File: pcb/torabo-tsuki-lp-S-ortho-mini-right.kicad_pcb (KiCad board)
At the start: 2 copper layers, 138.8 x 74 mm, 59 parts, among them J201 Conn_01x06_MountingPin, J202 FTSH-106-01-L-D-K, SW43 SW_Push, SW44 SW_Push, SW45 SW_Push, SW46 SW_Push, SW47 SW_Push, SW48 SW_Push, SW50 SW_Push, SW51 SW_Push, SW52 SW_Push, SW53 SW_Push, SW54 SW_Push, SW55 SW_Push, SW57 SW_Push, SW58 SW_Push, SW59 SW_Push, SW60 SW_Push, SW61 SW_Push, SW62 SW_Push, SW63 SW_Push, SW64 SW_Push, SW65 SW_Push, SW69 SW_Push, SW70 SW_Push, U201 XIAO nRF52840 Plus

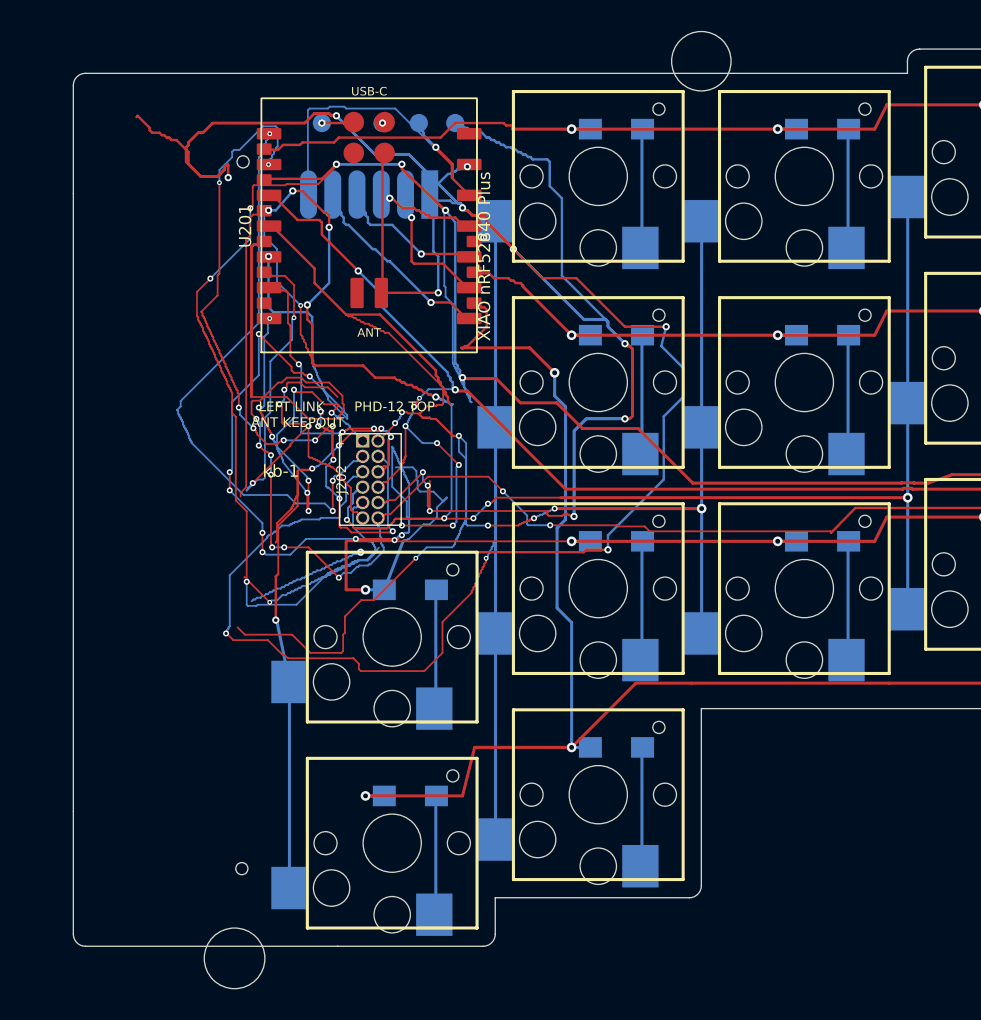
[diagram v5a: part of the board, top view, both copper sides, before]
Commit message: Shrink inner edges of split PCBs
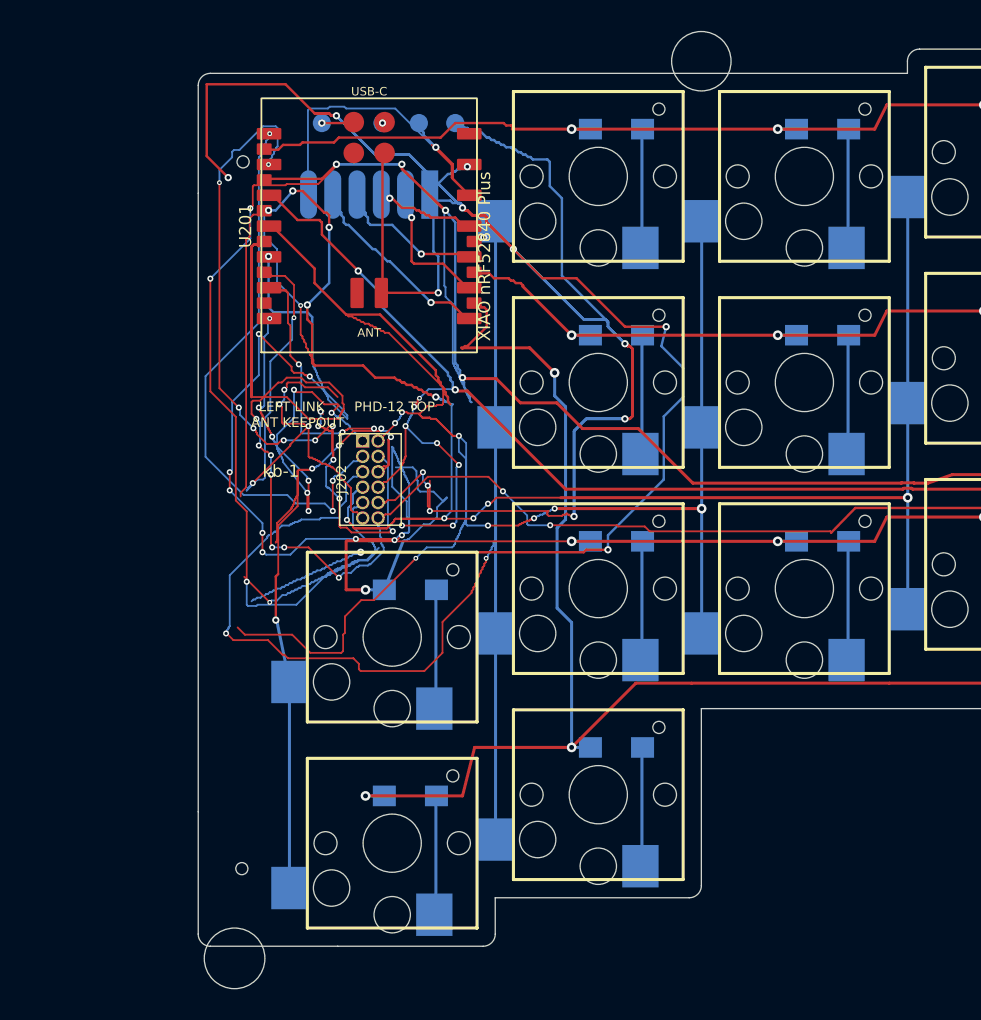
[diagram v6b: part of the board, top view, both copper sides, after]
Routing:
- net GND: track 327.2 -> 298.3 mm
- net /right/LROW0: track 49.2 -> 47.2 mm
- net /right/LROW1: track 67.6 -> 66.3 mm
- net /right/COL1: track 267.0 -> 266.1 mm
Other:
- board size 138.8 x 74 mm -> 128.5 x 74 mm

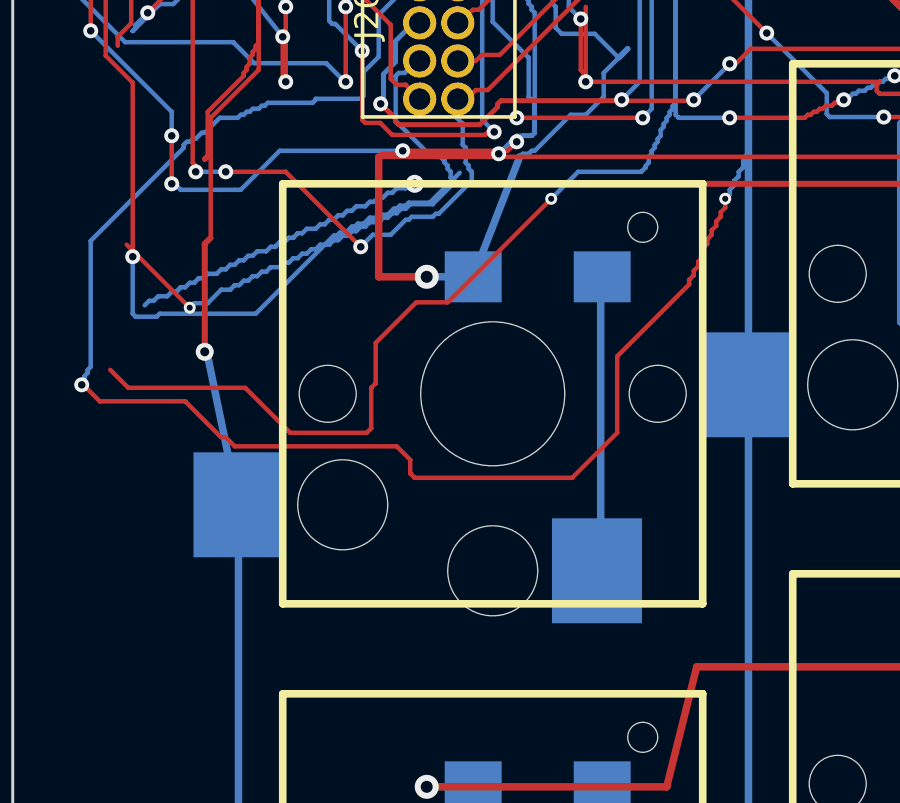
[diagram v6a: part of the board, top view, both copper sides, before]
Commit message: Remove key below right split connector
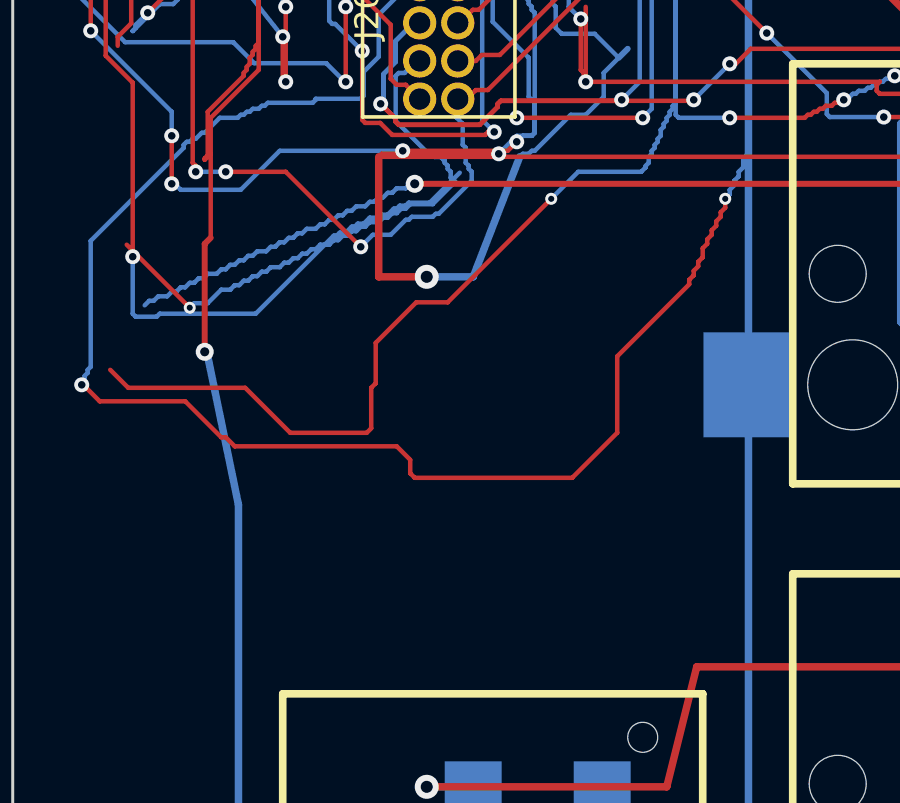
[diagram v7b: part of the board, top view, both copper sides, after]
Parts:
- removed D63: 1N4148W, Library:D_SOD-123_HandSoldering
- removed SW63: SW_Push, Library:CHOC_V2_SOCKET_HANDSOLDERING_17mm
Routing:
- net Net-(D63-K): track 9.87 -> 0.00 mm
